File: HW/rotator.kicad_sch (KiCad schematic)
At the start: 12 parts, among them J0 StepMotor_Connector, J1 Relay_Connector, J2 Generic_connector, J3 I2C_connector, J4 SPI_connector, J5 Power_connector, J6 12_IN, J7 12_OUT

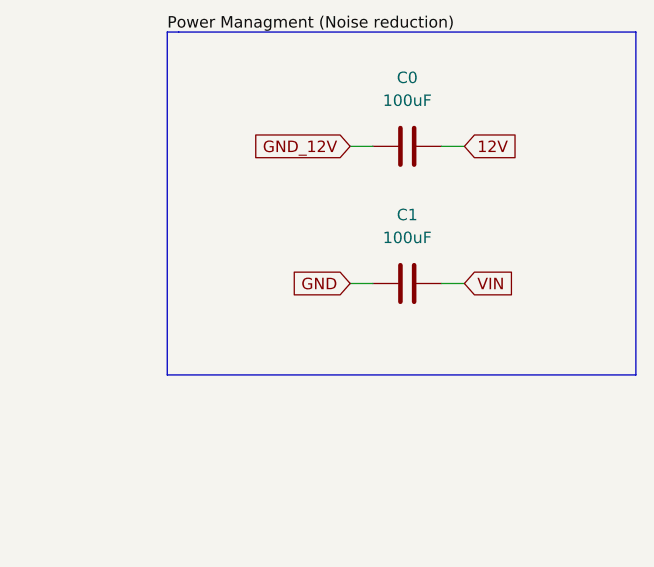
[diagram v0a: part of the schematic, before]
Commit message: Fixed C1 polarization in DPS
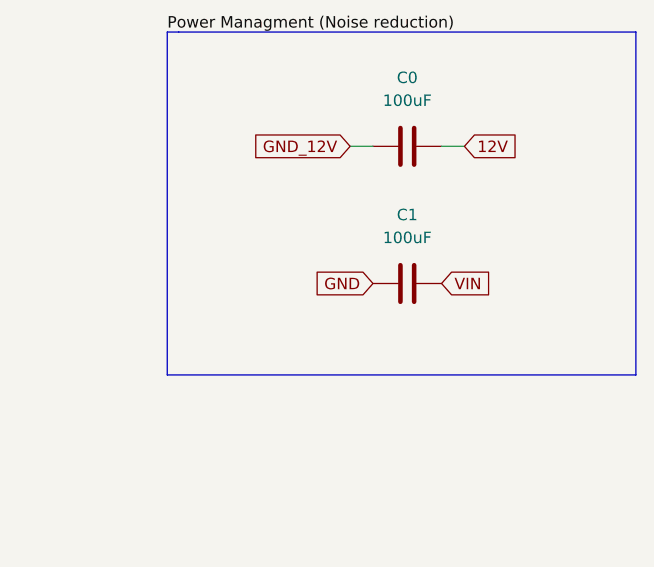
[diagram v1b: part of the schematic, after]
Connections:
- net GND: now also C1.2; no longer C1.1
- net VIN: now also C1.1; no longer C1.2
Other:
- moved on the sheet: C1
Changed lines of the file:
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@@
   (title_block
     (title "Arduino Sattelite Rotator")
-    (date "2022-07-06")
-    (rev "R1")
+    (date "2022-07-21")
+    (rev "2")
     (company "Lukáš Plevač")
     (comment 1 "Elevation linear motor")
@@
   (no_connect (at 71.12 76.2))
   (no_connect (at 71.12 78.74))
-  (wire (pts (xy 245.11 68.58) (xy 247.65 68.58))
-    (stroke (width 0) (type default) (color 0 0 0 0))
-  )
   (polyline (pts (xy 40.64 187.96) (xy 40.64 109.22))
-    (stroke (width 0) (type default) (color 0 0 0 0))
-  )
-  (wire (pts (xy 255.27 68.58) (xy 257.81 68.58))
     (stroke (width 0) (type default) (color 0 0 0 0))
   )
@@
     )
   )
-  (global_label "VIN" (shape input) (at 257.81 68.58 0) (fields_autoplaced)
-    (effects (font (size 1.27 1.27)) (justify left))
-    (property "Reference mezi listy" "${INTERSHEET_REFS}" (id 0) (at 263.2469 68.5006 0)
+  (global_label "VIN" (shape input) (at 255.27 68.58 0) (fields_autoplaced)
+    (effects (font (size 1.27 1.27)) (justify left))
+    (property "Reference mezi listy" "${INTERSHEET_REFS}" (id 0) (at 260.7069 68.5006 0)
       (effects (font (size 1.27 1.27)) (justify left) hide)
     )
@@
     )
   )
-  (global_label "GND" (shape input) (at 245.11 68.58 180) (fields_autoplaced)
-    (effects (font (size 1.27 1.27)) (justify right))
-    (property "Reference mezi listy" "${INTERSHEET_REFS}" (id 0) (at 238.8264 68.5006 0)
+  (global_label "GND" (shape input) (at 247.65 68.58 180) (fields_autoplaced)
+    (effects (font (size 1.27 1.27)) (justify right))
+    (property "Reference mezi listy" "${INTERSHEET_REFS}" (id 0) (at 241.3664 68.5006 0)
       (effects (font (size 1.27 1.27)) (justify right) hide)
     )
@@
     (pin "4")
   )
-  (symbol (lib_id "Device:C") (at 251.46 68.58 90) (unit 1)
+  (symbol (lib_id "Device:C") (at 251.46 68.58 270) (mirror x) (unit 1)
     (in_bom yes) (on_board yes) (fields_autoplaced)
     (property "Reference" "C1" (id 0) (at 251.46 60.96 90))
     (property "Value" "100uF" (id 1) (at 251.46 63.5 90))
-    (property "Footprint" "Capacitor_THT:CP_Radial_D6.3mm_P2.50mm" (id 2) (at 255.27 67.6148 0)
-      (effects (font (size 1.27 1.27)) hide)
-    )
+    (property "Footprint" "Capacitor_THT:CP_Radial_D6.3mm_P2.50mm" (id 2) (at 247.65 67.6148 0)
+      (effects (font (size 1.27 1.27)) hide)
+    )

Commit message: Fixed capacitator C0 polarization
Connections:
- net 12V: now also C0.1; no longer C0.2
- net GND_12V: now also C0.2; no longer C0.1
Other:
- moved on the sheet: C0
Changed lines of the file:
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@@
     (pin "7")
   )
-  (symbol (lib_id "Device:C") (at 251.46 53.34 90) (unit 1)
+  (symbol (lib_id "Device:C") (at 251.46 53.34 270) (unit 1)
     (in_bom yes) (on_board yes) (fields_autoplaced)
     (property "Reference" "C0" (id 0) (at 251.46 45.72 90))
     (property "Value" "100uF" (id 1) (at 251.46 48.26 90))
-    (property "Footprint" "Capacitor_THT:CP_Radial_D6.3mm_P2.50mm" (id 2) (at 255.27 52.3748 0)
+    (property "Footprint" "Capacitor_THT:CP_Radial_D6.3mm_P2.50mm" (id 2) (at 247.65 54.3052 0)
       (effects (font (size 1.27 1.27)) hide)
     )
